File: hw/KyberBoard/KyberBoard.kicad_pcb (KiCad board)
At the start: 4 copper layers, 60.7 x 27.2 mm, 79 parts, among them J1 282834-2, J2 282834-2, J3 OSTVN12A150, J4 15910060, Q1 STL120N4F6AG, Q2 SIS413DN-T1-GE3, Q3 SSM3K337R, Q4 STL76DN4LF7AG, Q5 SSM3K337R,LF, Q6 SSM3K337R,LF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

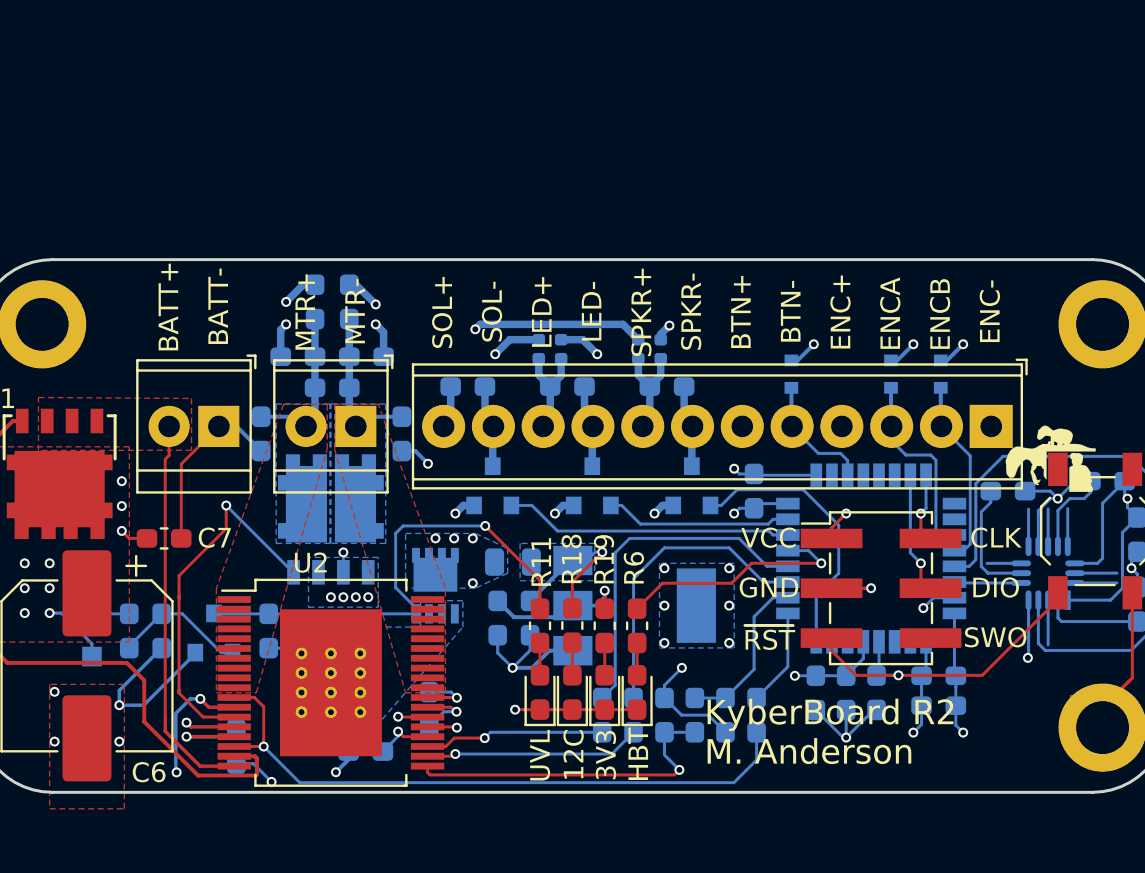
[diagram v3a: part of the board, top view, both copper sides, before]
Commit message: reworking pcb to be compatible with LED strip
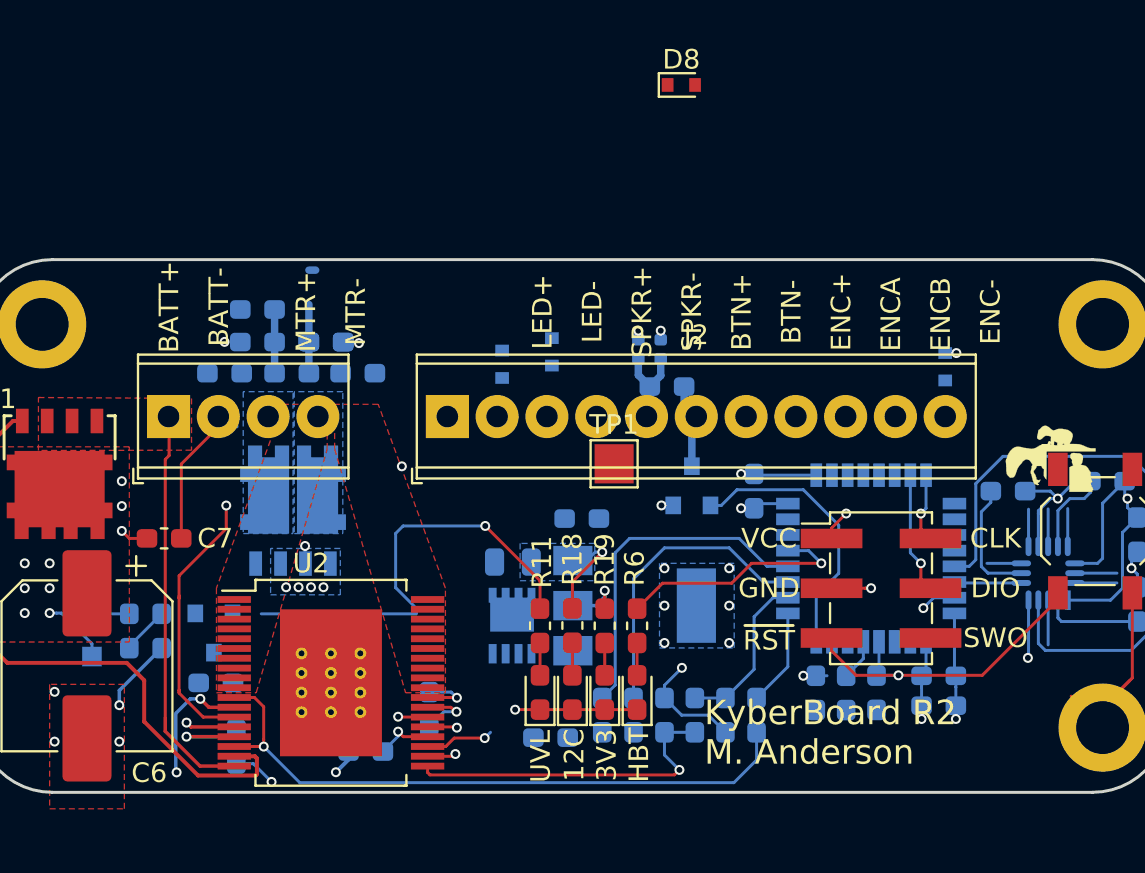
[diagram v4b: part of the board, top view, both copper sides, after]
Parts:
- removed D12: SDM2U30CSP-7, Diode_SMD:D_0603_1608Metric_Pad1.05x0.95mm_HandSolder
- removed the G*** at (163.0, 110.4)
- removed the G*** at (135.0, 110.7)
- removed the G*** at (176.3, 114.3)
- removed J3: OSTVN12A150, TerminalBlock_Phoenix:TerminalBlock_Phoenix_MPT-0,5-12-2.54_1x12_P2.54mm_Horizontal
- removed Q5, Q6: SSM3K337R,LF, Package_TO_SOT_SMD:SOT-23
- removed R14, R15: 0, Resistor_SMD:R_0402_1005Metric
- added TP1: TestPoint, TestPoint:TestPoint_Pad_2.0x2.0mm, F.Cu at (154.3, 98.4)
- D8: value SDM2U30CSP-7 -> BZT585B3V6T; footprint Diode_SMD:D_0603_1608Metric_Pad1.05x0.95mm_HandSolder -> Diode_SMD:D_SOD-523; moved to F.Cu
- J1: value 282834-2 -> Screw_Terminal_01x04; footprint TerminalBlock_TE-Connectivity:TerminalBlock_TE_282834-2_1x02_P2.54mm_Horizontal -> TerminalBlock_Phoenix:TerminalBlock_Phoenix_MPT-0,5-4-2.54_1x04_P2.54mm_Horizontal
- J2: value 282834-2 -> Screw_Terminal_01x11; footprint TerminalBlock_TE-Connectivity:TerminalBlock_TE_282834-2_1x02_P2.54mm_Horizontal -> TerminalBlock_Phoenix:TerminalBlock_Phoenix_MPT-0,5-11-2.54_1x11_P2.54mm_Horizontal
- moved D15 19.9 mm to (151.1, 92.7)
- moved D14 19.8 mm to (148.6, 93.3)
- moved D8 18.9 mm to (157.7, 79.1)
- moved D13 7.85 mm to (171.2, 93.5)
- moved C13 6.67 mm to (151.1, 112.4), turned to 0 degrees
- moved C12 5.72 mm to (152.7, 101.2), turned to 180 degrees
- moved J2 4.70 mm to (145.8, 96.0), turned to 0 degrees
- moved Q2 4.41 mm to (149.1, 106.7)
- moved C11 3.83 mm to (141.2, 93.8), turned to 0 degrees
- moved R8 3.78 mm to (134.0, 109.6), turned to 180 degrees
- moved C10 3.62 mm to (134.4, 93.8), turned to 180 degrees
- moved D6 2.96 mm to (136.1, 90.6), turned to 180 degrees
- moved J1 2.62 mm to (131.6, 96.0), turned to 0 degrees
- moved D7 2.37 mm to (139.6, 92.2), turned to 0 degrees
- moved D4 2.19 mm to (136.1, 92.2)
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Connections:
- D8 pad 1: +12V -> /LED_TX
- D8 pad 2: /SOL- -> GND
- J1 pad 1: GND -> /BATT+
- J1 pad 2: /BATT+ -> GND
- J2 pad 1: /MOT- -> +3V3
- J2 pad 2: /MOT+ -> /ENC_A
- U1 pad 14: /actuators/SIG_SOL -> Net-(U1-Pad14)
- U1 pad 15: /actuators/SIG_LED -> Net-(U1-Pad15)
- U1 pad 27: /ENC_A -> /ENC_B
- U1 pad 28: /ENC_B -> /ENC_A
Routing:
- net GND: track 110.9 -> 78.8 mm, vias 33 -> 25
- net /actuators/SIG_SOL: track 14.8 -> 0.00 mm
- net +12V: track 13.5 -> 0.46 mm, vias 6 -> 1
- net /ENC_B: track 10.6 -> 0.96 mm
- net /hbridge/PWM_MTR: track 11.0 -> 1.47 mm
- net /actuators/SIG_LED: track 9.52 -> 0.00 mm
- net /ENC_A: track 10.0 -> 1.03 mm
- net +3V3: track 48.3 -> 40.2 mm, vias 16 -> 15
- net /BTN: track 6.61 -> 0.30 mm
- net /LED+: track 5.91 -> 0.00 mm
- net /hbridge/INB: track 9.21 -> 3.51 mm
- net Net-(Q4-Pad4): track 19.3 -> 14.3 mm
- net /V_UNSAFE: track 9.87 -> 4.90 mm, vias 11 -> 10
- net /LED-: track 4.95 -> 0.00 mm
- net /MOT+: track 8.16 -> 3.51 mm, vias 0 -> 1
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- removed copper zone on B.Cu, net +12V
- removed copper zone on B.Cu, net /V_UNSAFE
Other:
- board text removed: "LED"
- board text removed: "SOL+"
- board text removed: "SOL-"
